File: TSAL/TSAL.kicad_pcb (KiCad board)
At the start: 2 copper layers, 100 x 56 mm, 134 parts, among them IC3 LTC6995IS6-2#TRMPBF, IC4 LTC6995IS6-2#TRMPBF, J1 Conn_SDC, J2 Conn_TSAL, J3 Conn_AIR, J4 Conn_01x02, J5 Conn_VI, J6 Conn_PRE, J7 Conn_HV, J8 Conn_control, K1 G2RL-2, Q1 2N7002, Q2 2N7002, Q3 2N7002, Q4 2N7002, Q5 DN2470K4, U1 AMC1351, U10 TLV7041DBV, U2 TLV7041DBV, U3 AS331KTR-G1, U4 AS331KTR-G1, U5 74LVC1G08, U6 AP2205-W5-7, U7 AP2205-W5-7, U8 AMC1351, U9 AP2204K-ADJ

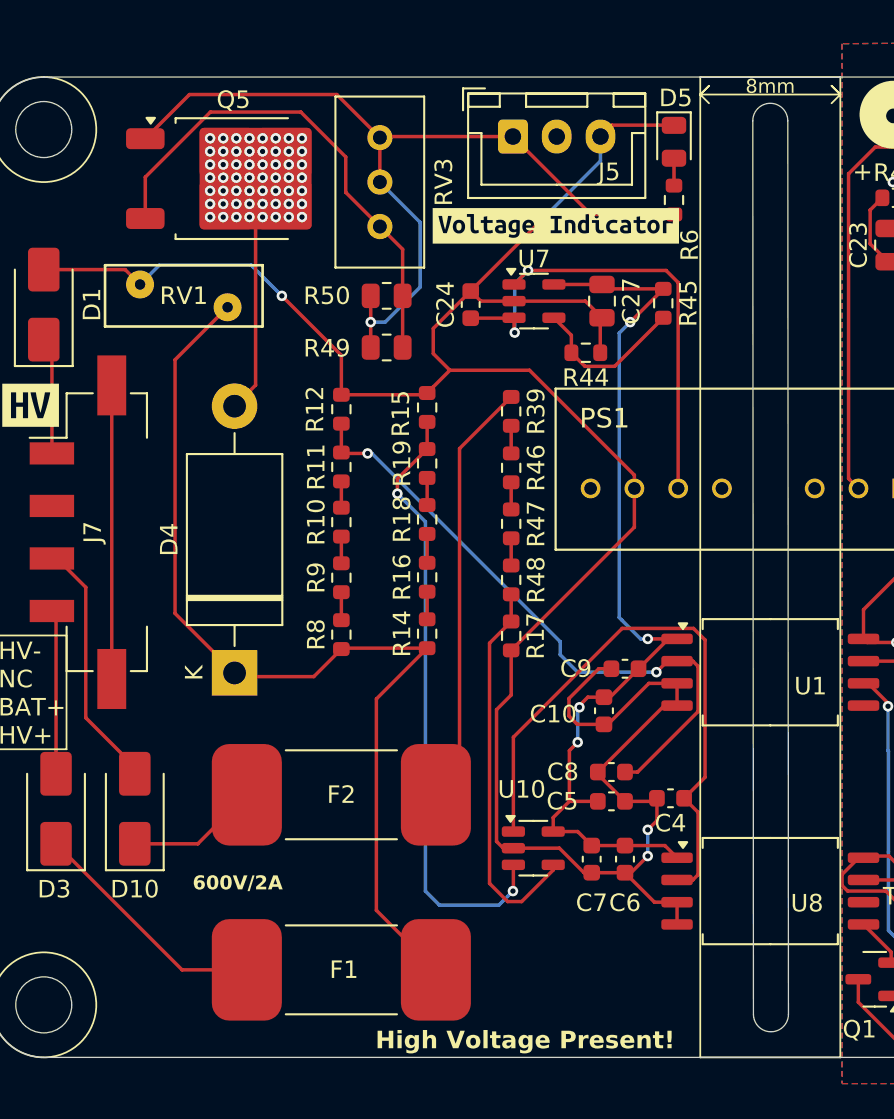
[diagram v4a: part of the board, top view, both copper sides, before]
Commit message: fix: replace NMOS and div resistors
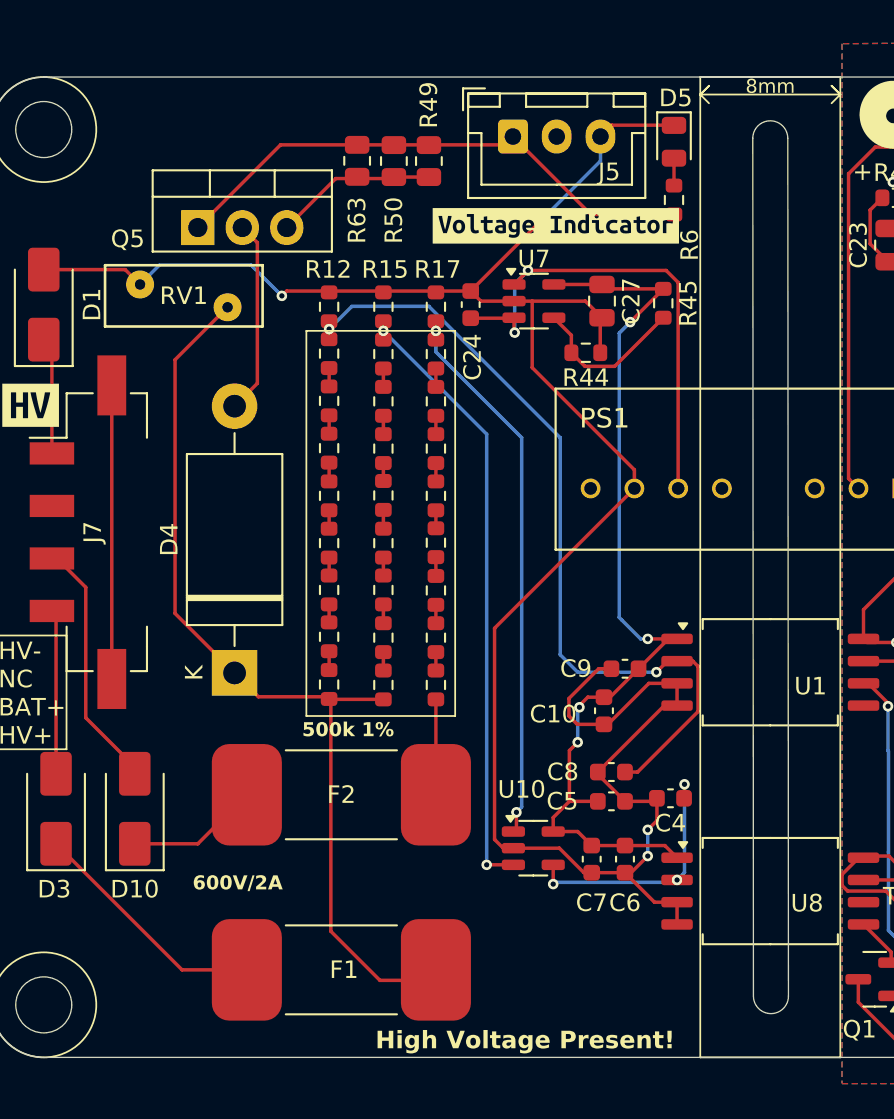
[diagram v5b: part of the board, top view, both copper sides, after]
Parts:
- removed RV3: 1k, Potentiometer_THT:Potentiometer_Bourns_3296W_Vertical
- added R51: 500k, Resistor_SMD:R_0603_1608Metric, F.Cu at (85.4, 53.9)
- added R52: 500k, Resistor_SMD:R_0603_1608Metric, F.Cu at (85.4, 51.2)
- added R53: 500k, Resistor_SMD:R_0603_1608Metric, F.Cu at (85.4, 48.5)
- added R54: 500k, Resistor_SMD:R_0603_1608Metric, F.Cu at (85.4, 45.8)
- added R55: 500k, Resistor_SMD:R_0603_1608Metric, F.Cu at (88.4, 64.7)
- added R56: 500k, Resistor_SMD:R_0603_1608Metric, F.Cu at (88.4, 62.0)
- added R57: 500k, Resistor_SMD:R_0603_1608Metric, F.Cu at (88.4, 59.3)
- added R58: 500k, Resistor_SMD:R_0603_1608Metric, F.Cu at (88.4, 56.6)
- added R59: 500k, Resistor_SMD:R_0603_1608Metric, F.Cu at (88.4, 53.9)
- added R60: 500k, Resistor_SMD:R_0603_1608Metric, F.Cu at (88.4, 51.2)
- added R61: 500k, Resistor_SMD:R_0603_1608Metric, F.Cu at (88.4, 48.5)
- added R62: 500k, Resistor_SMD:R_0603_1608Metric, F.Cu at (88.4, 45.8)
- added R63: 1k, Resistor_SMD:R_0805_2012Metric, F.Cu at (83.9, 34.8)
- Q5: footprint Package_TO_SOT_SMD:TO-252-2 -> Package_TO_SOT_THT:TO-220-3_Vertical
- R10, R11, R14, R16, R18, R19, R39, R46, R47, R48, R8, R9: value 1M -> 500k
- U10: value TLV7041DBV -> AS331KTR-G1
- moved R17 19.3 mm to (88.4, 43.1), turned to 90 degrees
- moved R39 17.2 mm to (85.4, 64.7), turned to 90 degrees
- moved R46 12.1 mm to (85.4, 62.0), turned to 90 degrees
- moved R49 10.9 mm to (88.0, 34.8), turned to 90 degrees
- moved R14 9.66 mm to (82.3, 53.9)
- moved R16 9.26 mm to (82.3, 51.2)
- moved R18 8.79 mm to (82.3, 48.5)
- moved R19 8.41 mm to (82.3, 45.8)
- moved R47 8.22 mm to (85.4, 59.3), turned to 90 degrees
- moved R50 7.71 mm to (86.0, 34.8), turned to 90 degrees
- moved R48 7.60 mm to (85.4, 56.6), turned to 90 degrees
- moved R15 6.27 mm to (85.4, 43.1)
- moved R12 5.89 mm to (82.3, 43.1)
- moved R11 4.41 mm to (82.3, 56.6)
- moved R10 3.94 mm to (82.3, 59.3)
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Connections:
- R11 pad 2: Net-(C8-Pad1) -> Net-(R11-Pad2)
- R14 pad 1: HV+ -> Net-(R11-Pad2)
- R19 pad 2: Net-(U10-+) -> Net-(C8-Pad1)
- R39 pad 1: BATT+ -> HV+
- R48 pad 2: Net-(U10--) -> Net-(R48-Pad2)
- U10 pad 1: Net-(C4-Pad1) -> Net-(U10--)
- U10 pad 4: Net-(U10--) -> Net-(C4-Pad1)
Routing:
- net Net-(C4-Pad1): track 34.8 -> 14.7 mm, vias 0 -> 3
- net Net-(Q5-S): track 28.6 -> 9.32 mm
- net Net-(J5-Pin_1): track 50.2 -> 31.2 mm, vias 1 -> 0
- net BATT+: track 24.5 -> 7.36 mm
- net unconnected-(J7-MountPin-PadMP)_1: track 16.8 -> 0.00 mm
- net unconnected-(J7-MountPin-PadMP): track 0.00 -> 16.8 mm
- net Net-(C8-Pad1): track 36.2 -> 46.6 mm
- net HV-: track 140.3 -> 130.5 mm
- net Net-(U10--): track 22.1 -> 31.9 mm, vias 0 -> 2
- net HV+: track 56.3 -> 53.4 mm
- net Net-(D4-A): track 13.5 -> 11.1 mm, vias 56 -> 0
- net Net-(R57-Pad2): track 0.00 -> 1.08 mm
- net Net-(R48-Pad2): track 0.00 -> 1.07 mm
- net Net-(R61-Pad2): track 0.00 -> 1.05 mm
- net Net-(R59-Pad2): track 0.00 -> 1.05 mm
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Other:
- outline, holes or cut-outs redrawn
- board text added: "500k 1%"

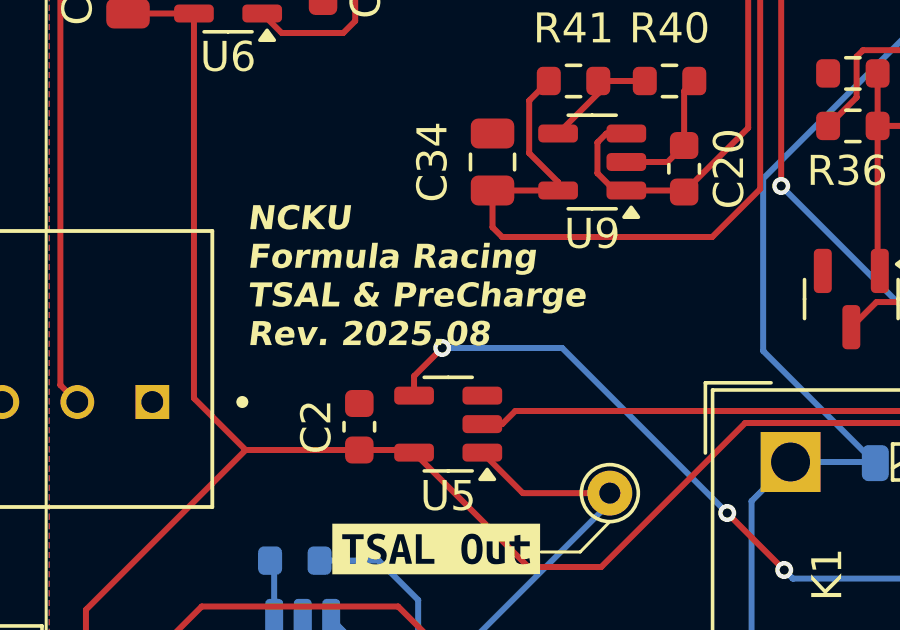
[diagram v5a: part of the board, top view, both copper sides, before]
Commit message: fix: update version of RTML
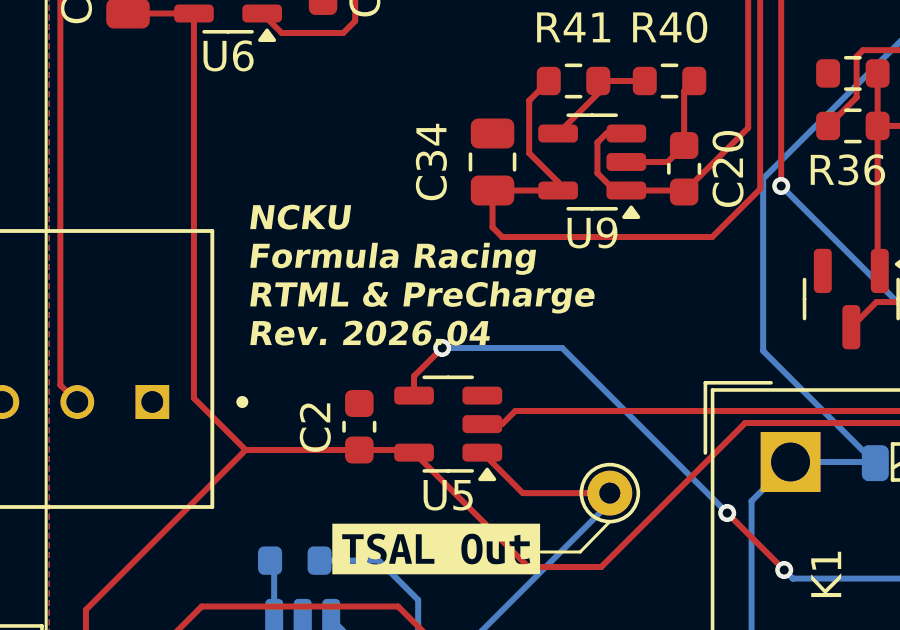
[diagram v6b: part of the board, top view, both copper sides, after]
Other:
- board text added: "NCKU Formula Racing RTML & PreCharge Rev. 2026.04"
- board text removed: "NCKU Formula Racing TSAL & PreCharge Rev. 2025.08"
